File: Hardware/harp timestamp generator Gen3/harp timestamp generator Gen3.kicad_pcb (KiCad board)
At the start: 4 copper layers, 124.5 x 80.4 mm, 153 parts, among them IC1 MCP73831, IC10 SN74LVC1G125DBVT, IC11 LP5951MFX-3.3/NOPB, IC12 SI8621BC, IC13 SI8621BC, IC14 SI8621BC, IC15 SI8621BC, IC16 SI8621BC, IC17 SI8621BC, IC18 SN74LVC1G125DBVT, IC19 SN74LVC1G125DBVT, IC2 USBLC6-2SC6, IC3 FT232RL-REEL, IC4 TPS2114, IC5 LP5951MFX-3.3/NOPB, IC6 ATXMEGA16A4U-A, IC7 M74VHC1GT126DF1G, IC8 M74VHC1GT126DF1G, IC9 M74VHC1GT126DF1G, Q1 RTU002P02T106, Q2 BC817-40W, Q3 SBC817, Q4 DMG1012UW, Q5 DMP2035U-7, T1 BC850, T10 BC850, T2 BC850, T3 BC850, T4 BC850, T5 BC850, T6 BC850, T7 BC850, T8 BC850, T9 BC850, X1 B2B-XH-A(LF)(SN)

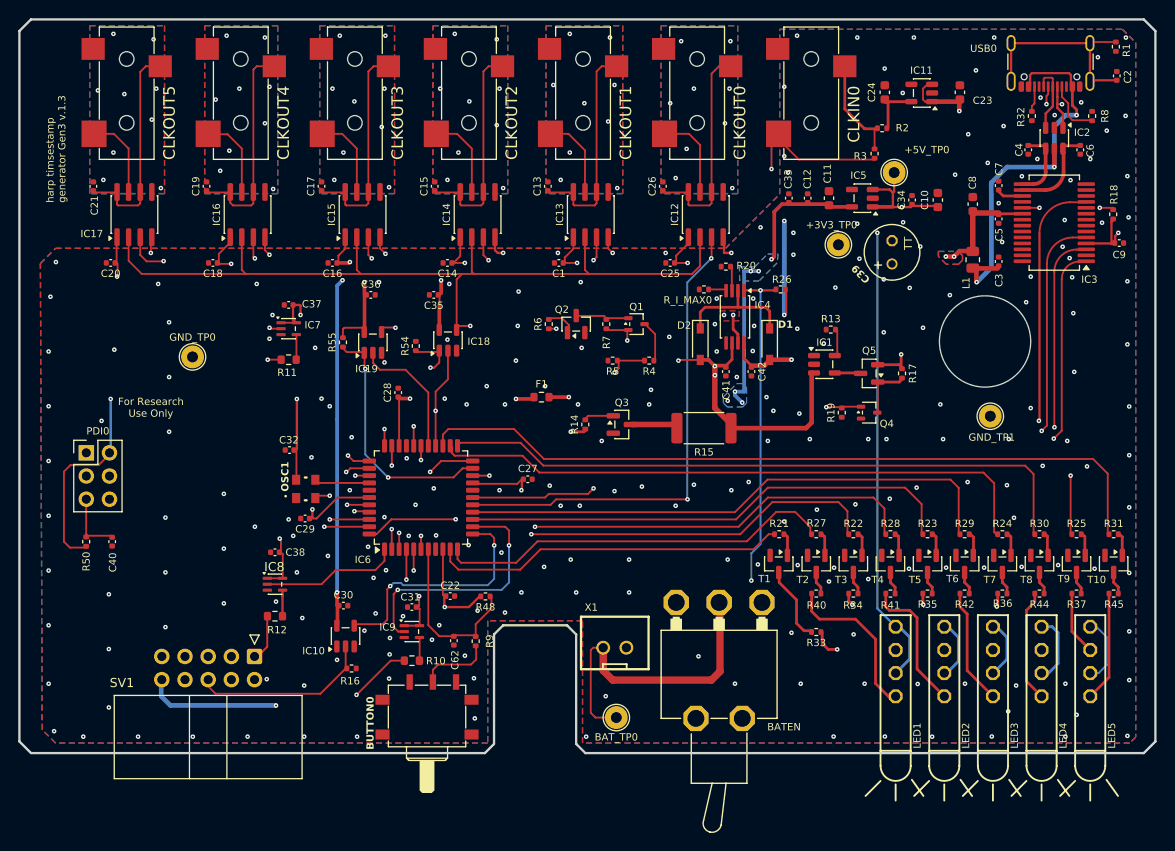
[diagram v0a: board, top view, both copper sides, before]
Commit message: ajuste posição ficha USB-C
> ajuste posição ficha USB-C
. actualizados manufacturing files:
   Gerbers & Drills & .d356 & P&P
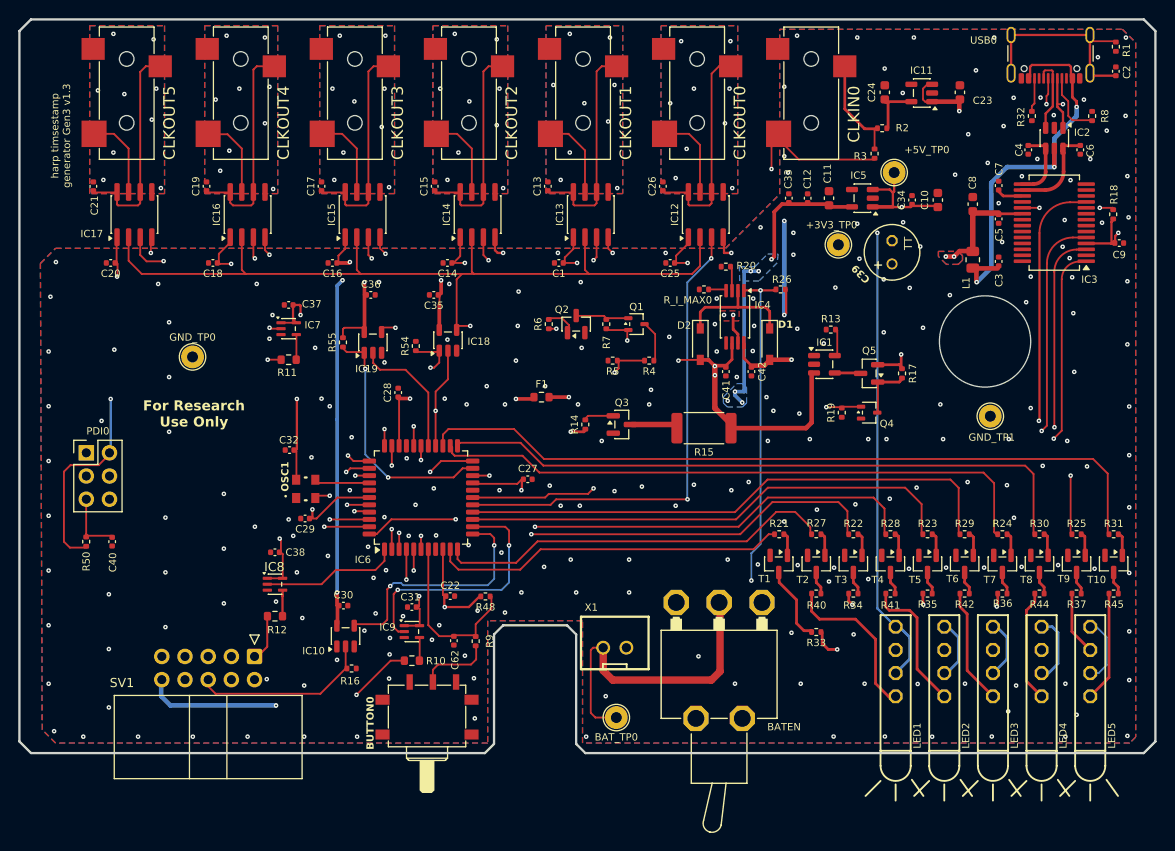
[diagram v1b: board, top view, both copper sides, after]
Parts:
- moved USB0 0.90 mm to (199.2, 67.6)
- moved C2 0.51 mm to (206.4, 70.5)
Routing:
- net Net-(IC2-I/O1-Pad1): track 8.58 -> 10.6 mm
- net Net-(USB0-SHIELD): track 22.8 -> 24.7 mm
- net Net-(USB0-CC2): track 2.84 -> 3.74 mm
- net Net-(USB0-CC1): track 6.33 -> 7.23 mm
- net Net-(IC2-I/O2-Pad3): track 7.26 -> 7.99 mm
- net GND: vias 228 -> 229
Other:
- board text added: "harp timsestamp generator Gen3 v1.3"
- board text removed: "harp timsestamp generator Gen3 v.1.3"
